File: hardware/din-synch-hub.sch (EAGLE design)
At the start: 47 parts, among them IC1 6N138, IC2 PIC12F1822SO08, IC3 4050D, IC4 REG1117, IC6 4050D, X1 DIN5PIN, X2 DIN5PIN, X3 DIN5PIN, X4 DIN5PIN, X5 DIN5PIN, X6 DIN5PIN

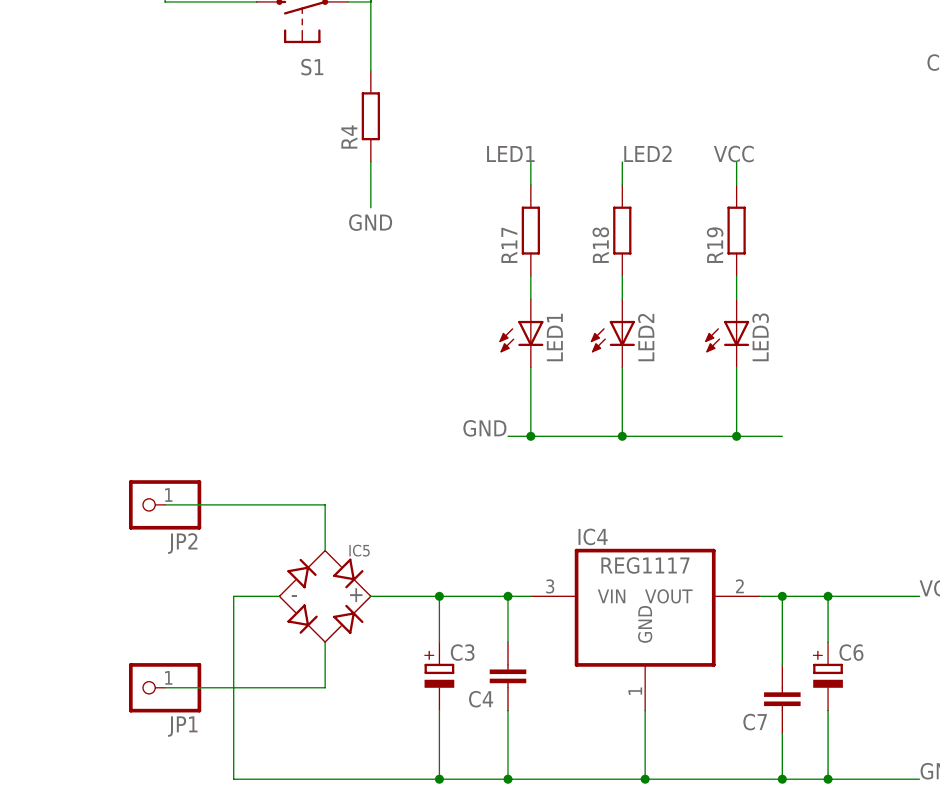
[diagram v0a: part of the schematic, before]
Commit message: added new power socket
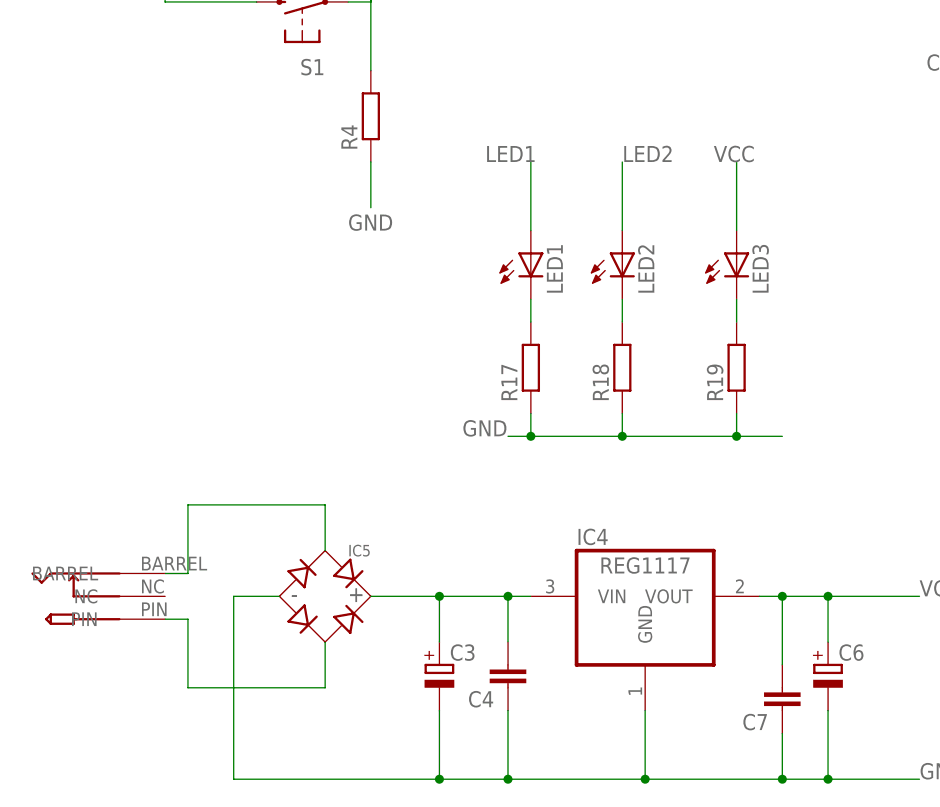
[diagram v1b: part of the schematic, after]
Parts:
- removed JP1, JP2: (no value), pinhead:PINHD-1X1
- added U$1: PWR_SOCKET_2_1MM, jason_eagle6:PWR_SOCKET_2_1MM
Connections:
- net GND: now also R17.1, R18.1, R19.1; no longer LED1.C, LED2.C, LED3.C
- net LED1: now also LED1.A; no longer R17.2
- net LED2: now also LED2.A; no longer R18.2
- net N$28: now also LED3.C, R19.2; no longer LED3.A, R19.1
- net N$31: now also LED2.C, R18.2; no longer LED1.A, R17.1
- net N$33: now also LED1.C, R17.2; no longer LED2.A, R18.1
- net N$36: now also U$1.PIN; no longer JP1.1
- net N$37: now also U$1.BARREL; no longer JP2.1
- net VCC: now also LED3.A; no longer R19.2
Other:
- moved on the sheet: LED1, LED2, LED3, R17, R18, R19
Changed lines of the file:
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@@
 <part name="IC4" library="burr-brown" deviceset="REG1117" device=""/>
 <part name="IC5" library="microbuilder" deviceset="BRIDGERECTIFIER" device=""/>
-<part name="JP1" library="pinhead" deviceset="PINHD-1X1" device=""/>
-<part name="JP2" library="pinhead" deviceset="PINHD-1X1" device=""/>
 <part name="C4" library="rcl" deviceset="C-EU" device="C0805"/>
 <part name="C7" library="rcl" deviceset="C-EU" device="C0805"/>
@@
 <part name="R19" library="rcl" deviceset="R-EU_" device="R0805"/>
 <part name="LED3" library="led" deviceset="LED" device="3MM"/>
+<part name="U$1" library="jason_eagle6" deviceset="PWR_SOCKET_2_1MM" device=""/>
 </parts>
 <sheets>
@@
 <instance part="R4" gate="G$1" x="33.02" y="38.1" rot="R90"/>
 <instance part="S1" gate="1" x="25.4" y="50.8" rot="R90"/>
-<instance part="LED1" gate="G$1" x="50.8" y="15.24"/>
-<instance part="R17" gate="G$1" x="50.8" y="25.4" rot="R90"/>
-<instance part="LED2" gate="G$1" x="60.96" y="15.24"/>
-<instance part="R18" gate="G$1" x="60.96" y="25.4" rot="R90"/>
+<instance part="LED1" gate="G$1" x="50.8" y="22.86"/>
+<instance part="R17" gate="G$1" x="50.8" y="10.16" rot="R90"/>
+<instance part="LED2" gate="G$1" x="60.96" y="22.86"/>
+<instance part="R18" gate="G$1" x="60.96" y="10.16" rot="R90"/>
 <instance part="IC4" gate="G$1" x="63.5" y="-15.24"/>
 <instance part="IC5" gate="G$1" x="27.94" y="-15.24"/>
-<instance part="JP1" gate="G$1" x="7.62" y="-25.4" rot="R180"/>
-<instance part="JP2" gate="G$1" x="7.62" y="-5.08" rot="R180"/>
 <instance part="C4" gate="G$1" x="48.26" y="-25.4" rot="R180"/>
 <instance part="C7" gate="G$1" x="78.74" y="-27.94" rot="R180"/>
 <instance part="C3" gate="G$1" x="40.64" y="-22.86"/>
 <instance part="C6" gate="G$1" x="83.82" y="-22.86"/>
-<instance part="R19" gate="G$1" x="73.66" y="25.4" rot="R90"/>
-<instance part="LED3" gate="G$1" x="73.66" y="15.24"/>
+<instance part="R19" gate="G$1" x="73.66" y="10.16" rot="R90"/>
+<instance part="LED3" gate="G$1" x="73.66" y="22.86"/>
+<instance part="U$1" gate="G$1" x="-2.54" y="-12.7" rot="MR180"/>
 </instances>
 <busses>
@@
 </segment>
 <segment>
-<pinref part="LED1" gate="G$1" pin="C"/>
-<wire x1="50.8" y1="10.16" x2="50.8" y2="2.54" width="0.1524" layer="91"/>
+<label x="43.18" y="2.54" size="1.778" layer="95"/>
 <wire x1="48.26" y1="2.54" x2="50.8" y2="2.54" width="0.1524" layer="91"/>
-<pinref part="LED2" gate="G$1" pin="C"/>
+<pinref part="R17" gate="G$1" pin="1"/>
 <wire x1="50.8" y1="2.54" x2="60.96" y2="2.54" width="0.1524" layer="91"/>
-<wire x1="60.96" y1="10.16" x2="60.96" y2="2.54" width="0.1524" layer="91"/>
+<wire x1="60.96" y1="2.54" x2="73.66" y2="2.54" width="0.1524" layer="91"/>
+<wire x1="73.66" y1="2.54" x2="78.74" y2="2.54" width="0.1524" layer="91"/>
+<wire x1="50.8" y1="5.08" x2="50.8" y2="2.54" width="0.1524" layer="91"/>
+<junction x="50.8" y="2.54"/>
+<pinref part="R18" gate="G$1" pin="1"/>
+<wire x1="60.96" y1="5.08" x2="60.96" y2="2.54" width="0.1524" layer="91"/>
 <junction x="60.96" y="2.54"/>
-<junction x="50.8" y="2.54"/>
-<label x="43.18" y="2.54" size="1.778" layer="95"/>
-<wire x1="60.96" y1="2.54" x2="73.66" y2="2.54" width="0.1524" layer="91"/>
-<pinref part="LED3" gate="G$1" pin="C"/>
-<wire x1="73.66" y1="2.54" x2="78.74" y2="2.54" width="0.1524" layer="91"/>
-<wire x1="73.66" y1="10.16" x2="73.66" y2="2.54" width="0.1524" layer="91"/>
+<pinref part="R19" gate="G$1" pin="1"/>
+<wire x1="73.66" y1="5.08" x2="73.66" y2="2.54" width="0.1524" layer="91"/>
 <junction x="73.66" y="2.54"/>
 </segment>
@@
 </segment>
 <segment>
-<pinref part="R19" gate="G$1" pin="2"/>
-<wire x1="73.66" y1="30.48" x2="73.66" y2="33.02" width="0.1524" layer="91"/>
 <label x="71.12" y="33.02" size="1.778" layer="95"/>
+<pinref part="LED3" gate="G$1" pin="A"/>
+<wire x1="73.66" y1="25.4" x2="73.66" y2="33.02" width="0.1524" layer="91"/>
 </segment>
 </net>
@@
 </segment>
 <segment>
-<pinref part="R17" gate="G$1" pin="2"/>
-<wire x1="50.8" y1="30.48" x2="50.8" y2="33.02" width="0.1524" layer="91"/>
 <label x="45.72" y="33.02" size="1.778" layer="95"/>
+<wire x1="50.8" y1="25.4" x2="50.8" y2="33.02" width="0.1524" layer="91"/>
+<pinref part="LED1" gate="G$1" pin="A"/>
 </segment>
 </net>
@@
 </segment>
 <segment>
-<pinref part="R18" gate="G$1" pin="2"/>
-<wire x1="60.96" y1="30.48" x2="60.96" y2="33.02" width="0.1524" layer="91"/>
 <label x="60.96" y="33.02" size="1.778" layer="95"/>
-</segment>
-</net>
-<net name="N$31" class="0">
-<segment>
-<pinref part="R17" gate="G$1" pin="1"/>
-<pinref part="LED1" gate="G$1" pin="A"/>
-<wire x1="50.8" y1="20.32" x2="50.8" y2="17.78" width="0.1524" layer="91"/>
-</segment>
-</net>
-<net name="N$33" class="0">
-<segment>
-<pinref part="R18" gate="G$1" pin="1"/>
+<wire x1="60.96" y1="25.4" x2="60.96" y2="33.02" width="0.1524" layer="91"/>
 <pinref part="LED2" gate="G$1" pin="A"/>
-<wire x1="60.96" y1="20.32" x2="60.96" y2="17.78" width="0.1524" layer="91"/>
 </segment>
 </net>
@@
 <net name="N$36" class="0">
 <segment>
-<pinref part="JP1" gate="G$1" pin="1"/>
 <pinref part="IC5" gate="G$1" pin="AC2"/>
-<wire x1="10.16" y1="-25.4" x2="27.94" y2="-25.4" width="0.1524" layer="91"/>
+<wire x1="12.7" y1="-25.4" x2="27.94" y2="-25.4" width="0.1524" layer="91"/>
 <wire x1="27.94" y1="-25.4" x2="27.94" y2="-20.32" width="0.1524" layer="91"/>
+<wire x1="12.7" y1="-17.78" x2="12.7" y2="-25.4" width="0.1524" layer="91"/>
+<pinref part="U$1" gate="G$1" pin="PIN"/>
+<wire x1="10.16" y1="-17.78" x2="12.7" y2="-17.78" width="0.1524" layer="91"/>
 </segment>
 </net>
 <net name="N$37" class="0">
 <segment>
-<pinref part="JP2" gate="G$1" pin="1"/>
 <pinref part="IC5" gate="G$1" pin="AC1"/>
-<wire x1="10.16" y1="-5.08" x2="27.94" y2="-5.08" width="0.1524" layer="91"/>
+<wire x1="12.7" y1="-5.08" x2="27.94" y2="-5.08" width="0.1524" layer="91"/>
 <wire x1="27.94" y1="-5.08" x2="27.94" y2="-10.16" width="0.1524" layer="91"/>
+<wire x1="12.7" y1="-12.7" x2="12.7" y2="-5.08" width="0.1524" layer="91"/>
+<pinref part="U$1" gate="G$1" pin="BARREL"/>
+<wire x1="10.16" y1="-12.7" x2="12.7" y2="-12.7" width="0.1524" layer="91"/>
 </segment>
 </net>
 <net name="N$28" class="0">
 <segment>
-<pinref part="R19" gate="G$1" pin="1"/>
-<pinref part="LED3" gate="G$1" pin="A"/>
-<wire x1="73.66" y1="20.32" x2="73.66" y2="17.78" width="0.1524" layer="91"/>
-</segment>
-</net>
+<pinref part="R19" gate="G$1" pin="2"/>
+<pinref part="LED3" gate="G$1" pin="C"/>
+<wire x1="73.66" y1="15.24" x2="73.66" y2="17.78" width="0.1524" layer="91"/>
+</segment>
+</net>
+<net name="N$31" class="0">
+<segment>
+<pinref part="R18" gate="G$1" pin="2"/>
+<pinref part="LED2" gate="G$1" pin="C"/>
+<wire x1="60.96" y1="15.24" x2="60.96" y2="17.78" width="0.1524" layer="91"/>
+</segment>
+</net>
+<net name="N$33" class="0">
+<segment>
+<pinref part="R17" gate="G$1" pin="2"/>
+<pinref part="LED1" gate="G$1" pin="C"/>
+<wire x1="50.8" y1="15.24" x2="50.8" y2="17.78" width="0.1524" layer="91"/>
+</segment>
+</net>

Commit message: major changes
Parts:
- added X7: VERTICAL_3_5MM_SOCKET, jason_eagle6:VERTICAL_3_5MM_SOCKET
- C3: device rcl:CPOL-EUE2,5-6E -> rcl:C-EUC0805
- C7: device rcl:C-EUC0805 -> rcl:CPOL-EUE2,5-6E
- IC1: value 6N138 -> 4050D; device optocoupler:6N138 -> 40xx:4050D
- IC2: value PIC12F1822SO08 -> REG1117; device jasons_stuff:PIC12F1822SO08 -> burr-brown:REG1117
- IC4: value REG1117 -> PIC12F1822SO08; device burr-brown:REG1117 -> jasons_stuff:PIC12F1822SO08
- IC5: value (none) -> 6N138; device microbuilder:BRIDGERECTIFIER -> optocoupler:6N138
- IC6: value 4050D -> (none); device 40xx:4050D -> microbuilder:BRIDGERECTIFIER
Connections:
- removed net IN: IC1.VO, IC2.RA5, R1.1
- removed net N$24: IC6F.O, R15.1
- new net MIDI: IC3F.I, IC4.RA5, IC5.VO, R16.1
- net CLK: now also IC1A.I, IC1C.I, IC1D.I, IC4.RA0/PGD; no longer IC2.RA0/PGD, IC3E.I, IC6A.I, IC6C.I, IC6E.I
- net GND: now also C1.1, C2.1, C3.2, C4.2, C7.-, IC1P.VSS, IC2.GND, IC3D.I, IC4.VSS, IC5.GND, IC6.-, R1.1, R17.2, R2.1, R3.1, S1.S, S1.S1; no longer C1.2, C2.2, C3.-, C4.1, C7.1, IC1.GND, IC2.VSS, IC4.GND, IC5.-, IC6P.VSS, R17.1, R18.1, R19.1, R3.2, R4.1
- net LED1: now also IC4.RA4; no longer IC2.RA4
- net LED2: now also IC4.RA2; no longer IC2.RA2
- net N$1: now also IC3F.O, R15.1; no longer IC3A.O, R6.1
- net N$10: now also R11.2; no longer R10.2
- net N$11: now also R12.2; no longer R9.2
- net N$12: now also IC1F.O, R10.1; no longer IC3F.O, R9.1
- net N$13: now also IC1E.O, R8.1; no longer IC6A.O, R12.1
- net N$14: now also R9.2; no longer R12.2
- net N$15: now also IC1D.O, R9.1; no longer IC6B.O, R11.1
- net N$16: now also R10.2; no longer R11.2
- net N$17: now also IC1A.O, R5.1; no longer IC6C.O, R14.1
- net N$18: now also R7.2; no longer R14.2
- net N$19: now also IC1B.O, R6.1; no longer IC6D.O, R13.1
- net N$2: now also R15.2, X1.5; no longer R6.2, X1.3
- net N$20: now also R8.2; no longer R13.2
- net N$21: now also IC1C.O, R7.1; no longer IC6E.O, R16.1
- net N$22: now also R5.2; no longer R16.2
- net N$23: now also R6.2; no longer R15.2
- net N$25: now also IC5.C, X7.3; no longer IC1.C
- net N$26: now also R19.1, X7.4; no longer R2.1
- net N$27: now also IC5.A, R19.2; no longer IC1.A, R2.2
- net N$28: now also R1.2; no longer R19.2
- net N$29: now also IC5.VB, R17.1; no longer IC1.VB, R3.1
- net N$3: now also IC3C.O, R13.1; no longer IC3B.O, R5.1
- net N$30: now also IC4.MCLR#/VPP/RA3, R4.1; no longer IC2.MCLR#/VPP/RA3, R4.2
- net N$31: now also R2.2; no longer R18.2
- net N$32: now also C2.2, C7.+, IC2.VIN, IC6.+; no longer C3.+, C4.2, IC4.VIN, IC5.+
- net N$33: now also R3.2; no longer R17.2
- net N$36: now also IC6.AC2; no longer IC5.AC2
- net N$37: now also IC6.AC1; no longer IC5.AC1
- net N$4: now also R18.1; no longer R5.2
- net N$5: now also IC3E.O, R14.1; no longer IC3C.O, R8.1
- net N$6: now also R13.2; no longer R8.2
- net N$7: now also IC3B.O, R12.1; no longer IC3D.O, R7.1
- net N$8: now also R14.2; no longer R7.2
- net N$9: now also IC3A.O, R11.1; no longer IC3E.O, R10.1
- net RUN: now also IC1B.I, IC1E.I, IC1F.I, IC3E.I, IC4.RA1/PGC; no longer IC2.RA1/PGC, IC3D.I, IC3F.I, IC6B.I, IC6D.I, IC6F.I
- net VCC: now also C1.2, C3.1, C4.1, IC1P.VDD, IC2.VOUT, IC4.VDD, IC5.VCC, R16.2, R18.2, R4.2; no longer C1.1, C2.1, C7.2, IC1.VCC, IC2.VDD, IC4.VOUT, IC6P.VDD, R1.2, S1.S, S1.S1
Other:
- note added: "DIN SYNC 1/2"
- note added: "DIN SYNC 3/4/5"
- note added: "Jason Hotchkiss"
- note added: "MIDI INPUT"
- note added: "MIDI THRU"
- note added: "POWER SUPPLY"
- note added: "PROCESSOR"
- note added: "Pin 1. Run Pin 3. Clock"
- note added: "SYNC-HOLE REV2"
- moved on the sheet: C1, C2, C4, C5, C6, IC3A, IC3B, IC3C, IC3D, IC3E, IC3F, IC3P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

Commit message: fix bug
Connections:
- net N$4: now also X1.4; no longer X1.1
